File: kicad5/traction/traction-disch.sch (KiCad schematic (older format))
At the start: 24 parts

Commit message: Rev A.4.2: third review round — 6 confirmed defects fixed (F52-F57)
- F52 FS26 buck passives to Table-106 selections: LCOR 2.2uH
  (CORE_LSEL_OTP=0x02; 4.7uH matched no listed value), V15S COUT
  2x22uF (~32uF eff vs 20-100 spec), CBTC 47nF, CBTP 22nF per
  CBOOT_PRE, VPRE COUT 2x22uF, CIN 22uF; effective-capacitance rows
  (bias/tol/temp derating) added to design-verify. VREF5 judged as a
  rail (CSB5+CMA1+CMA2 ~2.2uF eff, inside 1.1-3.3) per reviewer.
- F53 ACT45B CAN chokes: real windings are pins 1-4 and 2-3 (TDK
  circuit diagram) - both ports had transceiver CANH coupled onto
  external CANL; remapped, ERC asserts end-to-end pairing
- F54 ULDO15 completed: 220pF feed-forward across the 49.9k leg
  (fz 14.5kHz, onsemi 11-18kHz window), COUT 22uF
- F55 UEXD (ALM2402, 18V abs/16V rec) off raw VBATC -> behind ULDOEX
  12.1V (NCV4276C-ADJ); 24V jump start can no longer reach it
- F56 flyback switch BUK9Y14-80E (logic-level, VGS +/-10V DC) was
  outside abs-max at the 11.8V drive, masked by a 5.6V zener that
  conducted ~0.29A through every ON interval (~0.4W each). Now
  BUK7Y14-80E (standard-level +/-20V, same LFPAK56); zener repurposed
  to a dark 15V protective clamp
- F57 ordering code NCV4276CDTADJRKG (DT/ADJ were transposed)
- ASC-with-VCC1-open qualification documented (DESAT unavailable;
  double-fault given KL30-held V5GD) + IGN_SNS ADC disposition

Gates: 1691/1691 pins, ERC 779/0, design-verify 73P/3W/0F,
BOM Rs.70,090 @1k, 590 components, 192 lines.

Co-Authored-By: Claude Fable 5 <noreply@anthropic.com>
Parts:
- removed JCTL: HDR-1x4-2.54, HDR1x4, symbol traction-r1:HDR-1x4-2.54
- added RQDPD: 10k, R0603, symbol traction-r1:R
- CQD: renamed from RDIS1; value 470R -> 100nF; footprint AxialWW10W -> C0603; symbol traction-r1:R -> traction-r1:C; MPN WW-470R-10W-AX -> MLCC-100nF-25V
- JCTL: renamed from JDCN; value STUD-M6 -> HDR-1x4-2.54; footprint StudM6 -> HDR1x4; symbol traction-r1:TERM_1 -> traction-r1:HDR-1x4-2.54; MPN STUD-M6 -> HDR-1x4-2.54
- JDCP: renamed from RBLD1; value 27k -> STUD-M6; footprint R2512 -> StudM6; symbol traction-r1:R -> traction-r1:TERM_1; MPN R2512-27k-2W -> STUD-M6
- PSQD: renamed from QDIS; value HCM75S12T4K3 -> QA01C-18; footprint TO247-4L -> SIP7; symbol traction-r1:HCM75S12T4K3 -> traction-r1:QA01C-18; MPN HCM75S12T4K3 -> QA01C-18
- QDIS: renamed from UQD; value TLP152 -> HCM75S12T4K3; footprint SO6 -> TO247-4L; symbol traction-r1:TLP152 -> traction-r1:HCM75S12T4K3; LCSC C17255258 -> CLASS; MPN TLP152 -> HCM75S12T4K3
- RBLD9: renamed from PSQD; value QA01C-18 -> 27k; footprint SIP7 -> R2512; symbol traction-r1:QA01C-18 -> traction-r1:R; MPN QA01C-18 -> R2512-27k-2W
- RDIS4: renamed from RQDG; value 47R -> 470R; footprint R0603 -> AxialWW10W; MPN R0603-47R -> WW-470R-10W-AX
- RQDG: renamed from RQDL; value 470R -> 47R; MPN R0603-470R -> R0603-47R
- RQDL: renamed from RQDPD; value 10k -> 470R; MPN R0603-10k -> R0603-470R
- UQD: renamed from CQD; value 100nF -> TLP152; footprint C0603 -> SO6; symbol traction-r1:C -> traction-r1:TLP152; LCSC CLASS -> C17255258; MPN MLCC-100nF-25V -> TLP152
- renumbered JDCP to JDCN, RBLD10 to RBLD1, RBLD2 to RBLD10, RBLD3 to RBLD2, RBLD4 to RBLD3, RBLD5 to RBLD4, RBLD6 to RBLD5, RBLD7 to RBLD6, RBLD8 to RBLD7, RBLD9 to RBLD8, RDIS2 to RDIS1, RDIS3 to RDIS2, RDIS4 to RDIS3
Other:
- note added: "220 kW pk Discharge (HV, bolt-on) - 3 of 4 · rev A.4.2 · 3 sections · 24 components"
- note removed: "220 kW pk Discharge (HV, bolt-on) - 3 of 4 · rev A.4.1 · 3 sections · 24 components"
- moved on the sheet: JDCN, RBLD1, RBLD10, RBLD2, RBLD3, RBLD4, RBLD5, RBLD6, RBLD7, RBLD8, RDIS1, RDIS2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
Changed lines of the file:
@@
 Title "Traction Inverter — Discharge board (bolt-on, XM3 pattern)"
 Date "2026-09-09"
-Rev "A.4.1"
+Rev "A.4.2"
 Comp "Traction Inverter 220 kW pk - Discharge (HV, bolt-on), sheet 3 of 4"
 Comment1 "Inverter = Power board + Cap bank busbar + bolt-on Discharge board (all HV) + Control card (LV); safe state holds with any link lost"
@@
 $EndDescr
 Text Notes 600 7100 0    60   ~ 12
-220 kW pk Discharge (HV, bolt-on) - 3 of 4   ·   rev A.4.1   ·   3 sections   ·   24 components
+220 kW pk Discharge (HV, bolt-on) - 3 of 4   ·   rev A.4.2   ·   3 sections   ·   24 components
 Text Notes 600 7400 0    50   ~ 0
 NET NAMING: U<ref>_<PIN> = node at that IC pin   ·   R<stem>_M = series-pair midpoint   ·   R<stem>_<nm> = tap between R<stem>n/m   ·   all others are explicit design nets   ·   same name on another sheet = same net, joined only at the named connector/stud/tab
@@
 $Comp
 L traction-r1:HDR-1x4-2.54 JCTL
-U 1 1 5E00013C
+U 1 1 5E00013D
 P 9150 2100
 F 0 "JCTL" H 8750 1800 50  0000 R CNN
@@
 $Comp
 L traction-r1:TERM_1 JDCN
-U 1 1 5E00013D
+U 1 1 5E00013E
 P 8800 1550
 F 0 "JDCN" H 8800 1390 50  0000 C CNN
@@
 $Comp
 L traction-r1:TERM_1 JDCP
-U 1 1 5E00013E
+U 1 1 5E00013F
 P 8800 1150
 F 0 "JDCP" H 8800 990 50  0000 C CNN
@@
 $Comp
 L traction-r1:R RBLD1
-U 1 1 5E00013F
+U 1 1 5E000140
 P 8300 4400
 F 0 "RBLD1" H 8300 4240 50  0000 C CNN
@@
 $Comp
 L traction-r1:R RBLD10
-U 1 1 5E000140
+U 1 1 5E000141
 P 9800 6000
 F 0 "RBLD10" H 9800 5840 50  0000 C CNN
@@
 $Comp
 L traction-r1:R RBLD2
-U 1 1 5E000141
+U 1 1 5E000142
 P 8300 4800
 F 0 "RBLD2" H 8300 4640 50  0000 C CNN
@@
 $Comp
 L traction-r1:R RBLD3
-U 1 1 5E000142
+U 1 1 5E000143
 P 8300 5200
 F 0 "RBLD3" H 8300 5040 50  0000 C CNN
@@
 $Comp
 L traction-r1:R RBLD4
-U 1 1 5E000143
+U 1 1 5E000144
 P 8300 5600
 F 0 "RBLD4" H 8300 5440 50  0000 C CNN
@@
 $Comp
 L traction-r1:R RBLD5
-U 1 1 5E000144
+U 1 1 5E000145
 P 8300 6000
 F 0 "RBLD5" H 8300 5840 50  0000 C CNN
@@
 $Comp
 L traction-r1:R RBLD6
-U 1 1 5E000145
+U 1 1 5E000146
 P 9800 4400
 F 0 "RBLD6" H 9800 4240 50  0000 C CNN
@@
 $Comp
 L traction-r1:R RBLD7
-U 1 1 5E000146
+U 1 1 5E000147
 P 9800 4800
 F 0 "RBLD7" H 9800 4640 50  0000 C CNN
@@
 $Comp
 L traction-r1:R RBLD8
-U 1 1 5E000147
+U 1 1 5E000148
 P 9800 5200
 F 0 "RBLD8" H 9800 5040 50  0000 C CNN
@@
 $Comp
 L traction-r1:R RBLD9
-U 1 1 5E000148
+U 1 1 5E000149
 P 9800 5600
 F 0 "RBLD9" H 9800 5440 50  0000 C CNN
@@
 $Comp
 L traction-r1:QA01C-18 PSQD
-U 1 1 5E000149
+U 1 1 5E00014A
 P 2850 1800
 F 0 "PSQD" H 2450 1500 50  0000 R CNN
@@
 $Comp
 L traction-r1:HCM75S12T4K3 QDIS
-U 1 1 5E00014A
+U 1 1 5E00014B
 P 4850 1350
 F 0 "QDIS" H 4450 1000 50  0000 R CNN
@@
 $Comp
 L traction-r1:TLP152 UQD
-U 1 1 5E00014B
+U 1 1 5E00014C
 P 2850 3550
 F 0 "UQD" H 2450 3250 50  0000 R CNN
@@
 $Comp
 L traction-r1:C CQD
-U 1 1 5E00014C
+U 1 1 5E00014D
 P 2650 5850
 F 0 "CQD" H 2650 5690 50  0000 C CNN
@@
 $Comp
 L traction-r1:R RDIS1
-U 1 1 5E00014D
+U 1 1 5E00014E
 P 4650 2000
 F 0 "RDIS1" H 4650 1840 50  0000 C CNN
@@
 $Comp
 L traction-r1:R RDIS2
-U 1 1 5E00014E
+U 1 1 5E00014F
 P 4650 2400
 F 0 "RDIS2" H 4650 2240 50  0000 C CNN
@@
 $Comp
 L traction-r1:R RDIS3
-U 1 1 5E00014F
+U 1 1 5E000150
 P 4650 2800
 F 0 "RDIS3" H 4650 2640 50  0000 C CNN
@@
 $Comp
 L traction-r1:R RDIS4
-U 1 1 5E000150
+U 1 1 5E000151
 P 4650 3200
 F 0 "RDIS4" H 4650 3040 50  0000 C CNN
@@
 $Comp
 L traction-r1:R RQDG
-U 1 1 5E000151
+U 1 1 5E000152
 P 2650 5050
 F 0 "RQDG" H 2650 4890 50  0000 C CNN
@@
 $Comp
 L traction-r1:R RQDL
-U 1 1 5E000152
+U 1 1 5E000153
 P 2650 4650
 F 0 "RQDL" H 2650 4490 50  0000 C CNN
@@
 $Comp
 L traction-r1:R RQDPD
-U 1 1 5E000153
+U 1 1 5E000154
 P 2650 5450
 F 0 "RQDPD" H 2650 5290 50  0000 C CNN

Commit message: Rev A.4.3: fourth review round — LCOR reconciled, UB15 compensation (F58-F59)
- F58: LCOR netlist value became 2.2uH in A.4.2 but the parts-db class
  MPN kept printing IND-4.7uH-2A on the sheet and BOM - an assembler
  would fit the old part. MPN/desc now carry 2.2uH + the OTP pairing;
  value, sheet, BOM and CORE_LSEL_OTP=0x02 agree end-to-end.
- F59: TPS55340 COMP had only 10nF to ground (no zero; ~0deg screening
  phase margin in the CCM model). Series R3/C4 = 2k/100nF per TI
  8.2.1.2.11 + 470pF HF pole cap; RHPZ ~450kHz not limiting; measured
  Bode stays a bench gate.
- Narrative corrections per review: CBOOT_PRE 100nF was legal (Rev 6.1
  allows 22-100nF; 22nF kept as typ) - F52 log softened; VCC1 loss
  reclassified as a single initiating failure (UGDL open output) whose
  outcome is three-phase-open with ASC still commandable.

Gates: 1695/1695 pins, ERC 782/0, design-verify 75P/3W/0F,
BOM Rs.70,091 @1k, 592 components, 193 lines.

Co-Authored-By: Claude Fable 5 <noreply@anthropic.com>
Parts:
- removed JCTL: HDR-1x4-2.54, HDR1x4, symbol traction-r1:HDR-1x4-2.54
- removed JDCN: STUD-M6, StudM6, symbol traction-r1:TERM_1
- added RQDL: 470R, R0603, symbol traction-r1:R
- added RQDPD: 10k, R0603, symbol traction-r1:R
- CQD: renamed from RDIS2; value 470R -> 100nF; footprint AxialWW10W -> C0603; symbol traction-r1:R -> traction-r1:C; MPN WW-470R-10W-AX -> MLCC-100nF-25V
- JCTL: renamed from JDCP; value STUD-M6 -> HDR-1x4-2.54; footprint StudM6 -> HDR1x4; symbol traction-r1:TERM_1 -> traction-r1:HDR-1x4-2.54; MPN STUD-M6 -> HDR-1x4-2.54
- JDCN: renamed from RBLD1; value 27k -> STUD-M6; footprint R2512 -> StudM6; symbol traction-r1:R -> traction-r1:TERM_1; MPN R2512-27k-2W -> STUD-M6
- JDCP: renamed from RBLD10; value 27k -> STUD-M6; footprint R2512 -> StudM6; symbol traction-r1:R -> traction-r1:TERM_1; MPN R2512-27k-2W -> STUD-M6
- PSQD: renamed from UQD; value TLP152 -> QA01C-18; footprint SO6 -> SIP7; symbol traction-r1:TLP152 -> traction-r1:QA01C-18; LCSC C17255258 -> CLASS; MPN TLP152 -> QA01C-18
- QDIS: renamed from CQD; value 100nF -> HCM75S12T4K3; footprint C0603 -> TO247-4L; symbol traction-r1:C -> traction-r1:HCM75S12T4K3; MPN MLCC-100nF-25V -> HCM75S12T4K3
- RBLD8: renamed from PSQD; value QA01C-18 -> 27k; footprint SIP7 -> R2512; symbol traction-r1:QA01C-18 -> traction-r1:R; MPN QA01C-18 -> R2512-27k-2W
- RBLD9: renamed from QDIS; value HCM75S12T4K3 -> 27k; footprint TO247-4L -> R2512; symbol traction-r1:HCM75S12T4K3 -> traction-r1:R; MPN HCM75S12T4K3 -> R2512-27k-2W
- RDIS3: renamed from RQDG; value 47R -> 470R; footprint R0603 -> AxialWW10W; MPN R0603-47R -> WW-470R-10W-AX
- RDIS4: renamed from RQDL; footprint R0603 -> AxialWW10W; MPN R0603-470R -> WW-470R-10W-AX
- RQDG: renamed from RQDPD; value 10k -> 47R; MPN R0603-10k -> R0603-47R
- UQD: renamed from RDIS1; value 470R -> TLP152; footprint AxialWW10W -> SO6; symbol traction-r1:R -> traction-r1:TLP152; LCSC CLASS -> C17255258; MPN WW-470R-10W-AX -> TLP152
- renumbered RBLD2 to RBLD1, RBLD3 to RBLD10, RBLD4 to RBLD2, RBLD5 to RBLD3, RBLD6 to RBLD4, RBLD7 to RBLD5, RBLD8 to RBLD6, RBLD9 to RBLD7, RDIS3 to RDIS1, RDIS4 to RDIS2
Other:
- note added: "220 kW pk Discharge (HV, bolt-on) - 3 of 4 · rev A.4.3 · 3 sections · 24 components"
- note removed: "220 kW pk Discharge (HV, bolt-on) - 3 of 4 · rev A.4.2 · 3 sections · 24 components"
- moved on the sheet: RBLD1, RBLD10, RBLD2, RBLD3, RBLD4, RBLD5, RBLD6, RBLD7, RDIS1, RDIS2, RDIS3, RDIS4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
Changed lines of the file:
@@
 Title "Traction Inverter — Discharge board (bolt-on, XM3 pattern)"
 Date "2026-09-09"
-Rev "A.4.2"
+Rev "A.4.3"
 Comp "Traction Inverter 220 kW pk - Discharge (HV, bolt-on), sheet 3 of 4"
 Comment1 "Inverter = Power board + Cap bank busbar + bolt-on Discharge board (all HV) + Control card (LV); safe state holds with any link lost"
@@
 $EndDescr
 Text Notes 600 7100 0    60   ~ 12
-220 kW pk Discharge (HV, bolt-on) - 3 of 4   ·   rev A.4.2   ·   3 sections   ·   24 components
+220 kW pk Discharge (HV, bolt-on) - 3 of 4   ·   rev A.4.3   ·   3 sections   ·   24 components
 Text Notes 600 7400 0    50   ~ 0
 NET NAMING: U<ref>_<PIN> = node at that IC pin   ·   R<stem>_M = series-pair midpoint   ·   R<stem>_<nm> = tap between R<stem>n/m   ·   all others are explicit design nets   ·   same name on another sheet = same net, joined only at the named connector/stud/tab
@@
 $Comp
 L traction-r1:HDR-1x4-2.54 JCTL
-U 1 1 5E00013D
+U 1 1 5E00013F
 P 9150 2100
 F 0 "JCTL" H 8750 1800 50  0000 R CNN
@@
 $Comp
 L traction-r1:TERM_1 JDCN
-U 1 1 5E00013E
+U 1 1 5E000140
 P 8800 1550
 F 0 "JDCN" H 8800 1390 50  0000 C CNN
@@
 $Comp
 L traction-r1:TERM_1 JDCP
-U 1 1 5E00013F
+U 1 1 5E000141
 P 8800 1150
 F 0 "JDCP" H 8800 990 50  0000 C CNN
@@
 $Comp
 L traction-r1:R RBLD1
-U 1 1 5E000140
+U 1 1 5E000142
 P 8300 4400
 F 0 "RBLD1" H 8300 4240 50  0000 C CNN
@@
 $Comp
 L traction-r1:R RBLD10
-U 1 1 5E000141
+U 1 1 5E000143
 P 9800 6000
 F 0 "RBLD10" H 9800 5840 50  0000 C CNN
@@
 $Comp
 L traction-r1:R RBLD2
-U 1 1 5E000142
+U 1 1 5E000144
 P 8300 4800
 F 0 "RBLD2" H 8300 4640 50  0000 C CNN
@@
 $Comp
 L traction-r1:R RBLD3
-U 1 1 5E000143
+U 1 1 5E000145
 P 8300 5200
 F 0 "RBLD3" H 8300 5040 50  0000 C CNN
@@
 $Comp
 L traction-r1:R RBLD4
-U 1 1 5E000144
+U 1 1 5E000146
 P 8300 5600
 F 0 "RBLD4" H 8300 5440 50  0000 C CNN
@@
 $Comp
 L traction-r1:R RBLD5
-U 1 1 5E000145
+U 1 1 5E000147
 P 8300 6000
 F 0 "RBLD5" H 8300 5840 50  0000 C CNN
@@
 $Comp
 L traction-r1:R RBLD6
-U 1 1 5E000146
+U 1 1 5E000148
 P 9800 4400
 F 0 "RBLD6" H 9800 4240 50  0000 C CNN
@@
 $Comp
 L traction-r1:R RBLD7
-U 1 1 5E000147
+U 1 1 5E000149
 P 9800 4800
 F 0 "RBLD7" H 9800 4640 50  0000 C CNN
@@
 $Comp
 L traction-r1:R RBLD8
-U 1 1 5E000148
+U 1 1 5E00014A
 P 9800 5200
 F 0 "RBLD8" H 9800 5040 50  0000 C CNN
@@
 $Comp
 L traction-r1:R RBLD9
-U 1 1 5E000149
+U 1 1 5E00014B
 P 9800 5600
 F 0 "RBLD9" H 9800 5440 50  0000 C CNN
@@
 $Comp
 L traction-r1:QA01C-18 PSQD
-U 1 1 5E00014A
+U 1 1 5E00014C
 P 2850 1800
 F 0 "PSQD" H 2450 1500 50  0000 R CNN
@@
 $Comp
 L traction-r1:HCM75S12T4K3 QDIS
-U 1 1 5E00014B
+U 1 1 5E00014D
 P 4850 1350
 F 0 "QDIS" H 4450 1000 50  0000 R CNN
@@
 $Comp
 L traction-r1:TLP152 UQD
-U 1 1 5E00014C
+U 1 1 5E00014E
 P 2850 3550
 F 0 "UQD" H 2450 3250 50  0000 R CNN
@@
 $Comp
 L traction-r1:C CQD
-U 1 1 5E00014D
+U 1 1 5E00014F
 P 2650 5850
 F 0 "CQD" H 2650 5690 50  0000 C CNN
@@
 $Comp
 L traction-r1:R RDIS1
-U 1 1 5E00014E
+U 1 1 5E000150
 P 4650 2000
 F 0 "RDIS1" H 4650 1840 50  0000 C CNN
@@
 $Comp
 L traction-r1:R RDIS2
-U 1 1 5E00014F
+U 1 1 5E000151
 P 4650 2400
 F 0 "RDIS2" H 4650 2240 50  0000 C CNN
@@
 $Comp
 L traction-r1:R RDIS3
-U 1 1 5E000150
+U 1 1 5E000152
 P 4650 2800
 F 0 "RDIS3" H 4650 2640 50  0000 C CNN
@@
 $Comp
 L traction-r1:R RDIS4
-U 1 1 5E000151
+U 1 1 5E000153
 P 4650 3200
 F 0 "RDIS4" H 4650 3040 50  0000 C CNN
@@
 $Comp
 L traction-r1:R RQDG
-U 1 1 5E000152
+U 1 1 5E000154
 P 2650 5050
 F 0 "RQDG" H 2650 4890 50  0000 C CNN
@@
 $Comp
 L traction-r1:R RQDL
-U 1 1 5E000153
+U 1 1 5E000155
 P 2650 4650
 F 0 "RQDL" H 2650 4490 50  0000 C CNN
@@
 $Comp
 L traction-r1:R RQDPD
-U 1 1 5E000154
+U 1 1 5E000156
 P 2650 5450
 F 0 "RQDPD" H 2650 5290 50  0000 C CNN

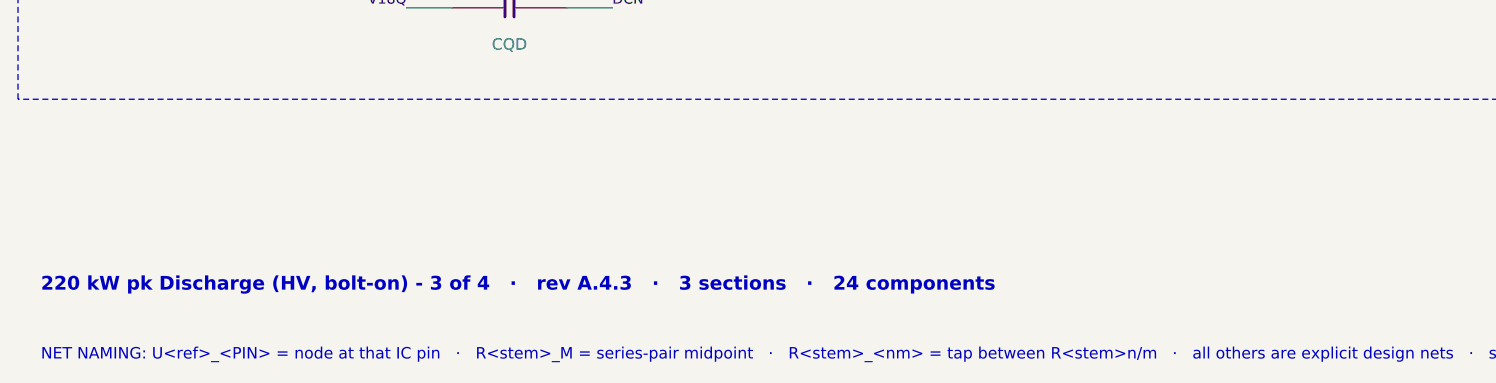
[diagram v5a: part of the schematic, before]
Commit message: Rev A.4.4: round five — bind class MPNs to real parts, pin FS26 OTP config
No electrical change. Procurement closure of the review's remaining
generic identifiers, each verified against its manufacturer datasheet:

- LCOR -> Coilcraft XAL4020-222MEC (2.2uH molded, AEC-Q200; values
  read from the XAL4000 datasheet, now in docs/datasheets)
- LB15 + LSBC -> XAL4040-103MEC (one 10uH line item for both; LSBC
  pairing with FPRE_OTP=450kHz documented per the FS26 DS)
- PS5B/PS5C -> Murata MGJ2D150505SC (+5V output used) behind an
  explicit PO gate: verify reinforced-insulation characterization at
  850VDC working and the SIP-7 pin map before ordering
- RECOM R15P05S evaluated and REJECTED during binding: its 6.4kV is a
  1-second test voltage; IEC 62368-1 insulation grade is BASIC at
  250VACrms working - fails the 850V barrier rule. Rejection recorded
  in design-basis 11e and the BOM row so it cannot be substituted in.
- FS26 OTP configuration pinned as design-basis 8a table (VPRE 6.0V,
  FPRE 450kHz, CORE_LSEL=0x02, VCORE 1.5V, LDO1/2 3.3/5.0V, VMONEXT
  0.8V ref, TRK slots off, VBST disabled, WK2PD/IO2PD set) - the
  ordering step must match it; the family label alone is not evidence.

Gates unchanged: 1695/1695 pins, ERC 782/0, design-verify 75P/3W/0F,
sim-verify 18P/1W/0F. BOM Rs.70,934 @1k with real part prices.

Co-Authored-By: Claude Fable 5 <noreply@anthropic.com>
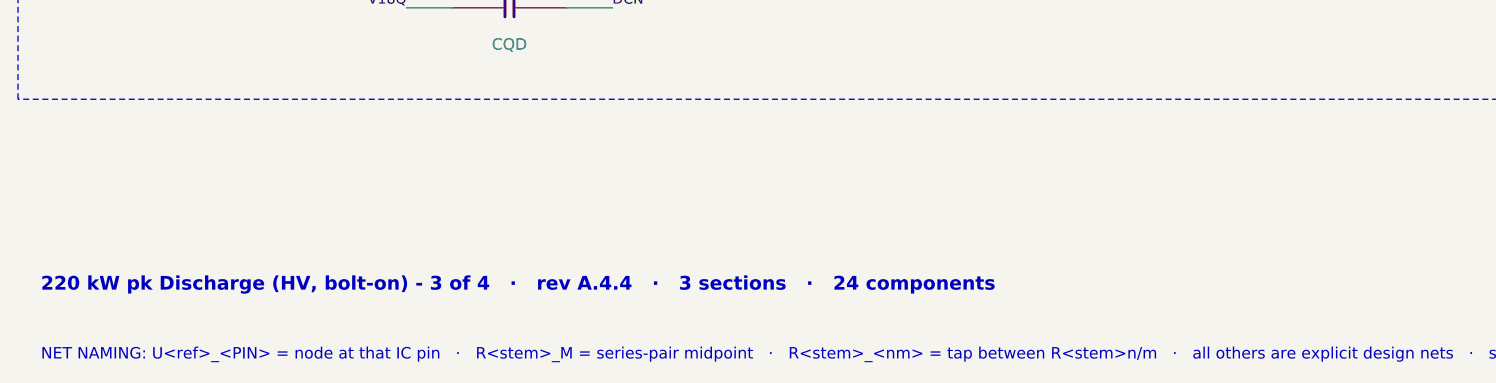
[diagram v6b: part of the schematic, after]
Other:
- note added: "220 kW pk Discharge (HV, bolt-on) - 3 of 4 · rev A.4.4 · 3 sections · 24 components"
- note removed: "220 kW pk Discharge (HV, bolt-on) - 3 of 4 · rev A.4.3 · 3 sections · 24 components"
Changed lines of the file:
@@
 Title "Traction Inverter — Discharge board (bolt-on, XM3 pattern)"
 Date "2026-09-09"
-Rev "A.4.3"
+Rev "A.4.4"
 Comp "Traction Inverter 220 kW pk - Discharge (HV, bolt-on), sheet 3 of 4"
 Comment1 "Inverter = Power board + Cap bank busbar + bolt-on Discharge board (all HV) + Control card (LV); safe state holds with any link lost"
@@
 $EndDescr
 Text Notes 600 7100 0    60   ~ 12
-220 kW pk Discharge (HV, bolt-on) - 3 of 4   ·   rev A.4.3   ·   3 sections   ·   24 components
+220 kW pk Discharge (HV, bolt-on) - 3 of 4   ·   rev A.4.4   ·   3 sections   ·   24 components
 Text Notes 600 7400 0    50   ~ 0
 NET NAMING: U<ref>_<PIN> = node at that IC pin   ·   R<stem>_M = series-pair midpoint   ·   R<stem>_<nm> = tap between R<stem>n/m   ·   all others are explicit design nets   ·   same name on another sheet = same net, joined only at the named connector/stud/tab
